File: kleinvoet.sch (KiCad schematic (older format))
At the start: 43 parts, among them CN1 Arduino_Conn, CN2 Arduino_Conn, CN3 Arduino_Conn, J1 Conn_ST_STDC14, SW1 RESET, SW2 RESET, U1 STM32F446RETx, U2 NOR Flash, Y1 12 MHz, Y2 32.768 kHz

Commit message: PCB Layout Checkpoint
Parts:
- added FB9: BLM15HD102SN1, Inductor_SMD:L_0402_1005Metric, symbol Device:Ferrite_Bead_Small
- SW2: value RESET -> USER
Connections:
- net +3V3: no longer CB6.1
- net A0: no longer CN1.1 (Pin_1)
- net A1: now also FB9.1; no longer CN1.2 (Pin_2)
- net A2: no longer CN1.3 (Pin_3)
- net A3: no longer CN1.4 (Pin_4)
- net A4: no longer CN1.5 (Pin_5)
- net A5: no longer CN1.6 (Pin_6)
- net D0: no longer CN3.8 (Pin_8)
- net D1: no longer CN3.7 (Pin_7)
- net D10: no longer CN2.8 (Pin_8)
- net D11: no longer CN2.7 (Pin_7)
- net D12: no longer CN2.6 (Pin_6)
- net D13: no longer CN2.5 (Pin_5)
- net D14: no longer CN2.2 (Pin_2)
- net D15: no longer CN2.1 (Pin_1)
- net D2: no longer CN3.6 (Pin_6)
- net D3: no longer CN3.5 (Pin_5)
- net D4: no longer CN3.4 (Pin_4)
- net D5: no longer CN3.3 (Pin_3)
- net D6: no longer CN3.2 (Pin_2)
- net D7: no longer CN3.1 (Pin_1)
- net D8: no longer CN2.10 (Pin_10)
- net D9: no longer CN2.9 (Pin_9)
- net USR_BTN: now also U1.28 (PB2)
- net VDD: now also CB6.1
- net ADC_~CS: now reaches U1.37 (PC6)
- new net GNSS_Module/GPS_RX: FB9.2
- no-connect marks 6 -> 26
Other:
- moved on the sheet: CB6
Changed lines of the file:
@@
-	1    0    0    -1
-$EndComp
-$Comp
-L Device:C_Small CB6
-U 1 1 5F161171
-P 5250 6000
-F 0 "CB6" H 5200 6300 50  0000 L CNN
-F 1 "100n" H 5150 6200 50  0000 L CNN
-F 2 "Capacitor_SMD:C_0603_1608Metric_Pad1.05x0.95mm_HandSolder" H 5250 6000 50  0001 C CNN
-F 3 "~" H 5250 6000 50  0001 C CNN
-F 4 "C0603C104M5RACTU" H 5250 6000 50  0001 C CNN "MPN"
-F 5 "KEMET" H 5250 6000 50  0001 C CNN "Mfr."
-	1    5250 6000
 	1    0    0    -1
 $EndComp
@@
 Wire Wire Line
 	4850 5900 5050 5900
-Connection ~ 5050 5900
-Wire Wire Line
-	5050 5900 5250 5900
 Wire Wire Line
 	4550 6100 4350 6100
 Connection ~ 4850 6100
-Connection ~ 5050 6100
 Wire Wire Line
 	5050 6100 4850 6100
-Wire Wire Line
-	5250 6100 5050 6100
 Wire Wire Line
 	4350 5900 4150 5900
@@
 	-1   0    0    -1
 $EndComp
-Text Label 3050 6800 0    50   ~ 0
-A0
-Text Label 3050 6900 0    50   ~ 0
-A1
-Text Label 3050 7000 0    50   ~ 0
-A2
-Text Label 3050 7100 0    50   ~ 0
-A3
-Text Label 3050 7200 0    50   ~ 0
-A4
-Text Label 3050 7300 0    50   ~ 0
-A5
 $Comp
 L Connector_Generic:Conn_01x10 CN2
@@
 	1    0    0    -1
 $EndComp
-Text Label 3750 6650 2    50   ~ 0
-D15
-Text Label 3750 6750 2    50   ~ 0
-D14
-Text Label 3750 7050 2    50   ~ 0
-D13
-Text Label 3750 7150 2    50   ~ 0
-D12
-Text Label 3750 7250 2    50   ~ 0
-D11
-Text Label 3750 7350 2    50   ~ 0
-D10
-Text Label 3750 7450 2    50   ~ 0
-D9
-Text Label 3750 7550 2    50   ~ 0
-D8
 $Comp
 L Connector_Generic:Conn_01x08 CN3
@@
 	1    0    0    -1
 $EndComp
-Text Label 4400 6750 2    50   ~ 0
-D7
-Text Label 4400 6850 2    50   ~ 0
-D6
-Text Label 4400 6950 2    50   ~ 0
-D5
-Text Label 4400 7050 2    50   ~ 0
-D4
-Text Label 4400 7150 2    50   ~ 0
-D3
-Text Label 4400 7250 2    50   ~ 0
-D2
-Text Label 4400 7350 2    50   ~ 0
-D1
-Text Label 4400 7450 2    50   ~ 0
-D0
 Wire Notes Line
 	2700 6500 4900 6500
@@
 Text Notes 5250 6500 0    50   ~ 10
 Status LEDs
-$Comp
-L MCU_ST_STM32F4:STM32F446RETx U1
-U 1 1 5EF8E42C
-P 4750 2950
-F 0 "U1" H 4250 1200 50  0000 C CNN
-F 1 "STM32F446RETx" H 5350 1200 50  0000 C CNN
-F 2 "Package_QFP:LQFP-64_10x10mm_P0.5mm" H 4150 1250 50  0001 R CNN
-F 3 "http://www.st.com/st-web-ui/static/active/en/resource/technical/document/datasheet/DM00141306.pdf" H 4750 2950 50  0001 C CNN
-F 4 "STM32F446RCT6" H 4750 2950 50  0001 C CNN "MPN"
-F 5 "STMicroelectronics" H 4750 2950 50  0001 C CNN "Mfr."
-	1    4750 2950
-	1    0    0    -1
-$EndComp
 $Comp
 L power:+3.3VA #PWR016
@@
 Wire Wire Line
 	2600 1500 2400 1500
-Wire Wire Line
-	2600 1700 2400 1700
 $Sheet
 S 1400 1350 1000 500
@@
 Wire Wire Line
 	2600 2200 2400 2200
-$Comp
-L power:GND #PWR03
-U 1 1 5EFC01A8
-P 2600 2550
-F 0 "#PWR03" H 2600 2300 50  0001 C CNN
-F 1 "GND" H 2605 2377 50  0000 C CNN
-F 2 "" H 2600 2550 50  0001 C CNN
-F 3 "" H 2600 2550 50  0001 C CNN
-	1    2600 2550
-	1    0    0    -1
-$EndComp
-Wire Wire Line
-	2600 2550 2600 2500
 Wire Wire Line
 	2600 2500 2400 2500
@@
 Wire Wire Line
 	1200 1750 1400 1750
+Text Label 5650 2350 0    50   ~ 0
+SDIO_WP
 Text Label 5650 2250 0    50   ~ 0
-SDIO_WP
-Text Label 5650 2350 0    50   ~ 0
 SDIO_CD
 Wire Wire Line
@@
 NoConn ~ 5450 2950
 NoConn ~ 5450 3850
-NoConn ~ 4050 3650
 Text Label 10650 5400 0    50   ~ 0
 OSC_LSE_IN
@@
 L power:VDD #PWR018
 U 1 1 5EEDB6FA
-P 5650 5900
-F 0 "#PWR018" H 5650 5750 50  0001 C CNN
-F 1 "VDD" H 5665 6073 50  0000 C CNN
-F 2 "" H 5650 5900 50  0001 C CNN
-F 3 "" H 5650 5900 50  0001 C CNN
-	1    5650 5900
+P 5550 5900
+F 0 "#PWR018" H 5550 5750 50  0001 C CNN
+F 1 "VDD" H 5565 6073 50  0000 C CNN
+F 2 "" H 5550 5900 50  0001 C CNN
+F 3 "" H 5550 5900 50  0001 C CNN
+	1    5550 5900
 	1    0    0    -1
 $EndComp
@@
 L power:GND #PWR019
 U 1 1 5EEDC419
-P 5650 6100
-F 0 "#PWR019" H 5650 5850 50  0001 C CNN
-F 1 "GND" H 5655 5927 50  0000 C CNN
-F 2 "" H 5650 6100 50  0001 C CNN
-F 3 "" H 5650 6100 50  0001 C CNN
-	1    5650 6100
+P 5550 6100
+F 0 "#PWR019" H 5550 5850 50  0001 C CNN
+F 1 "GND" H 5555 5927 50  0000 C CNN
+F 2 "" H 5550 6100 50  0001 C CNN
+F 3 "" H 5550 6100 50  0001 C CNN
+	1    5550 6100
 	1    0    0    -1
 $EndComp
@@
 Wire Wire Line
 	4050 4250 3850 4250
-NoConn ~ 5450 3350
 $Comp
 L Switch:SW_Push SW2
@@
 P 8800 1250
 F 0 "SW2" V 8800 1398 50  0000 L CNN
-F 1 "RESET" V 8845 1398 50  0001 L CNN
+F 1 "USER" V 8845 1398 50  0001 L CNN
 F 2 "grootvoet:SW_SPST_PTS647" H 8800 1450 50  0001 C CNN
 F 3 "~" H 8800 1450 50  0001 C CNN
@@
 Wire Wire Line
 	1200 2600 1400 2600
+$Comp
+L Device:Ferrite_Bead_Small FB9
+U 1 1 5F0F97AE
+P 2500 1700
+AR Path="/5F0F97AE" Ref="FB9"  Part="1"
+AR Path="/5EDF3693/5F0F97AE" Ref="FB?"  Part="1"
+F 0 "FB9" V 2650 1700 50  0000 C CNN
+F 1 "BLM15HD102SN1" V 2550 2050 50  0001 C CNN
+F 2 "Inductor_SMD:L_0402_1005Metric" V 2430 1700 50  0001 C CNN
+F 3 "~" H 2500 1700 50  0001 C CNN
+F 4 "BLM15HD102SN1D" V 2500 1700 50  0001 C CNN "MPN"
+F 5 "Murata Electronics" H 2500 1700 50  0001 C CNN "Mfr."
+	1    2500 1700
+	0    1    1    0
+$EndComp
+$Comp
+L Device:C_Small CB6
+U 1 1 5F161171
+P 5450 6000
+F 0 "CB6" H 5250 6100 50  0000 L CNN
+F 1 "100n" H 5200 6000 50  0000 L CNN
+F 2 "Capacitor_SMD:C_0603_1608Metric_Pad1.05x0.95mm_HandSolder" H 5450 6000 50  0001 C CNN
+F 3 "~" H 5450 6000 50  0001 C CNN
+F 4 "C0603C104M5RACTU" H 5450 6000 50  0001 C CNN "MPN"
+F 5 "KEMET" H 5450 6000 50  0001 C CNN "Mfr."
+	1    5450 6000
+	1    0    0    -1
+$EndComp
+Wire Wire Line
+	5450 5900 5550 5900
+Connection ~ 5550 5900
+Wire Wire Line
+	5550 5900 5650 5900
+Wire Wire Line
+	5650 6100 5550 6100
+Connection ~ 5550 6100
+Wire Wire Line
+	5550 6100 5450 6100
+Text Label 3850 3650 2    50   ~ 0
+ADC_~CS
+Wire Wire Line
+	4050 3650 3850 3650
+Text Label 2600 2500 0    50   ~ 0
+ADC_~CS
+Text Label 5650 3350 0    50   ~ 0
+USR_BTN
+$Comp
+L MCU_ST_STM32F4:STM32F446RETx U1
+U 1 1 5EF8E42C
+P 4750 2950
+F 0 "U1" H 4250 1200 50  0000 C CNN
+F 1 "STM32F446RETx" H 5350 1200 50  0000 C CNN
+F 2 "Package_QFP:LQFP-64_10x10mm_P0.5mm" H 4150 1250 50  0001 R CNN
+F 3 "http://www.st.com/st-web-ui/static/active/en/resource/technical/document/datasheet/DM00141306.pdf" H 4750 2950 50  0001 C CNN
+F 4 "STM32F446RCT6" H 4750 2950 50  0001 C CNN "MPN"
+F 5 "STMicroelectronics" H 4750 2950 50  0001 C CNN "Mfr."
+	1    4750 2950
+	1    0    0    -1
+$EndComp
+Wire Wire Line
+	5650 3350 5450 3350
+NoConn ~ 4400 6750
+NoConn ~ 4400 6850
+NoConn ~ 4400 6950
+NoConn ~ 4400 7050
+NoConn ~ 4400 7150
+NoConn ~ 4400 7250
+NoConn ~ 4400 7350
+NoConn ~ 4400 7450
+NoConn ~ 3750 7550
+NoConn ~ 3750 7450
+NoConn ~ 3750 7350
+NoConn ~ 3750 7250
+NoConn ~ 3750 7150
+NoConn ~ 3750 7050
+NoConn ~ 3750 6750
+NoConn ~ 3750 6650
+NoConn ~ 3050 6800
+NoConn ~ 3050 6900
+NoConn ~ 3050 7000
+NoConn ~ 3050 7100
+NoConn ~ 3050 7200
+NoConn ~ 3050 7300
 $EndSCHEMATC

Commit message: Major Commit with Final PCB Design
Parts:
- removed C3: 1u, Capacitor_SMD:C_0603_1608Metric_Pad1.05x0.95mm_HandSolder, symbol Device:C_Small
- removed CN1: Arduino_Conn, Connector_PinHeader_2.54mm:PinHeader_1x06_P2.54mm_Vertical, symbol Connector_Generic:Conn_01x06
- removed CN2: Arduino_Conn, Connector_PinHeader_2.54mm:PinHeader_1x10_P2.54mm_Vertical, symbol Connector_Generic:Conn_01x10
- removed CN3: Arduino_Conn, Connector_PinHeader_2.54mm:PinHeader_1x08_P2.54mm_Vertical, symbol Connector_Generic:Conn_01x08
- removed D2: GREEN, LED_SMD:LED_0603_1608Metric_Pad1.05x0.95mm_HandSolder, symbol Device:LED_Small
- removed D3: YELLOW, LED_SMD:LED_0603_1608Metric_Pad1.05x0.95mm_HandSolder, symbol Device:LED_Small
- removed R3, R4: 2.2k, Resistor_SMD:R_0603_1608Metric_Pad1.05x0.95mm_HandSolder, symbol Device:R_Small
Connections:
- net VDD is gone; now on net +3V3: CB6.1, U1.1 (VBAT)
- net D13: no longer R2.1
- net D15: now also CB9.1, SW2.1
- net RTC_CAL: no longer U1.2 (PC13)
- net LED_STATUS: now reaches U1.50 (PA15)
- net LED_STATUS: now also R2.1
- net D9 renamed ADC_CLK
- net GPS_WAKE: no longer names the net of U1.10 (PC2)
- net GPS_~SAFEBOOT: no longer names the net of U1.11 (PC3)
- removed net USR_BTN: CB9.1, SW2.1, U1.28 (PB2)
- no-connect marks 26 -> 7
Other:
- note removed: "Arduino Connectors"
- moved on the sheet: CB1, CB6, D1, R2, SW1

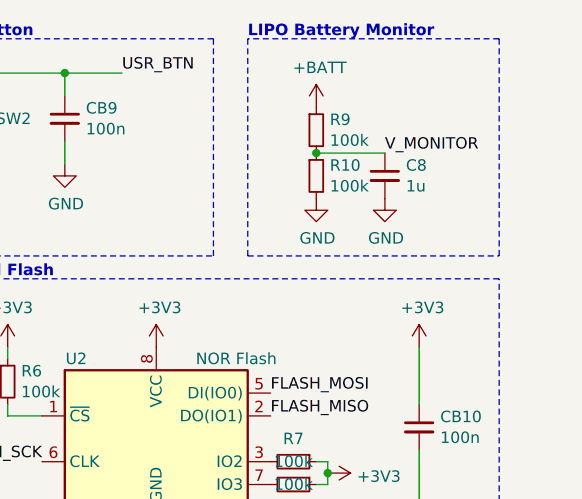
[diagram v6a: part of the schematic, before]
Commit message: Merge 'feature/mic-board'
Split out Sensor_board to own project for easier panelising later.
Allows also for better independent development.

Squashed commit of the following:
===============================================
commit 5c89ddf7514428c762fb7c211bc44fe947092eb1
Author: CM Geldenhuys <20198329@sun.ac.za>
Date:   Wed Oct 21 14:34:31 2020 +0200

    Add emblem

commit bbe0a53b49b0ec3aa4e2f65424c556ce99509fe4
Author: CM Geldenhuys <20198329@sun.ac.za>
Date:   Wed Oct 21 11:03:40 2020 +0200

    Misc.

commit b3172de48a622d4a7c8e9fb13a381d32a0990437
Author: CM Geldenhuys <20198329@sun.ac.za>
Date:   Wed Oct 21 08:26:42 2020 +0200

    Update BOM

commit e4c5b39694adfe3b823840b4cd3bc00d306b52fc
Author: CM Geldenhuys <20198329@sun.ac.za>
Date:   Wed Oct 21 07:26:34 2020 +0200

    Update Footprint & part num.

commit 6125562d7501cc555d98682860bdd64678a2fa40
Author: CM Geldenhuys <20198329@sun.ac.za>
Date:   Tue Oct 20 15:41:10 2020 +0200

    Misc. TODOs

commit 1431b8ace7af2c4960b7d9361ce6fcca694d3a38
Author: CM Geldenhuys <20198329@sun.ac.za>
Date:   Tue Oct 20 11:22:04 2020 +0200

    Update passives (fuse + Vsense)

commit 8105b403ec058cf7267c739b2e244ad8880c475f
Author: CM Geldenhuys <20198329@sun.ac.za>
Date:   Tue Oct 20 11:02:06 2020 +0200

    Flip GPS labels

commit f34b34dca70ce235e33188df7f6c69707ad79c9c
Author: CM Geldenhuys <20198329@sun.ac.za>
Date:   Tue Oct 20 10:58:45 2020 +0200

    Swap out ST-Link Conn

commit 1669b3f99c1cffa6c87811843550b346cfb9297e
Author: CM Geldenhuys <20198329@sun.ac.za>
Date:   Tue Oct 20 09:57:40 2020 +0200

    Update Sch with new compensation

commit dde033bb3cbd48a104931da2f1a7f681a8f96ac4
Author: CM Geldenhuys <20198329@sun.ac.za>
Date:   Tue Oct 20 09:55:04 2020 +0200

    Compensate for preamp loading on ADC driver

commit 2ddbd04fb1deccaa72131771362207bd14115936
Author: CM Geldenhuys <20198329@sun.ac.za>
Date:   Tue Oct 20 09:38:09 2020 +0200

    Compensate for buffer output impedance

commit 2f74ea7d6b171bacb6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
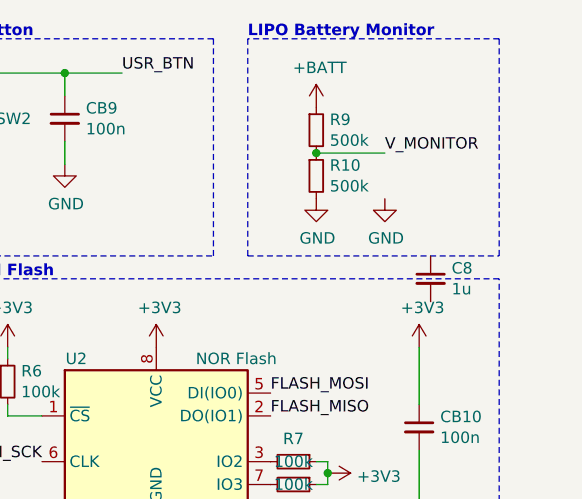
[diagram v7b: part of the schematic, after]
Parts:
- C4, C5, C6, C7, C8, C9, CB1, CB10, CB2, CB3, CB4, CB5, CB6, CB7, CB8, CB9: footprint Capacitor_SMD:C_0603_1608Metric_Pad1.05x0.95mm_HandSolder -> Capacitor_SMD:C_0603_1608Metric_Pad1.08x0.95mm_HandSolder
- J1: footprint Connector_PinHeader_1.27mm:PinHeader_2x07_P1.27mm_Vertical -> grootvoet:SAMTEC-FTSH-107-01-X-D
- R10, R9: value 100k -> 500k; MPN RC0603FR-07100KL -> (none); Mfr. Yageo -> (none)
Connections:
- net ADC1_IN9: no longer C8.1
- net GND: no longer C8.2
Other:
- moved on the sheet: C8
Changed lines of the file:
@@
 $Descr A4 11693 8268
 encoding utf-8
-Sheet 1 17
+Sheet 1 13
 Title "Kleinvoet"
 Date "2020-06-11"
@@
 F 0 "CB2" H 4300 6300 50  0000 L CNN
 F 1 "100n" H 4250 6200 50  0000 L CNN
-F 2 "Capacitor_SMD:C_0603_1608Metric_Pad1.05x0.95mm_HandSolder" H 4350 6000 50  0001 C CNN
+F 2 "Capacitor_SMD:C_0603_1608Metric_Pad1.08x0.95mm_HandSolder" H 4350 6000 50  0001 C CNN
 F 3 "~" H 4350 6000 50  0001 C CNN
 F 4 "C0603C104M5RACTU" H 4350 6000 50  0001 C CNN "MPN"
@@
 F 0 "CB7" H 7942 5841 50  0000 L CNN
 F 1 "100n" H 7942 5750 50  0000 L CNN
-F 2 "Capacitor_SMD:C_0603_1608Metric_Pad1.05x0.95mm_HandSolder" H 7850 5750 50  0001 C CNN
+F 2 "Capacitor_SMD:C_0603_1608Metric_Pad1.08x0.95mm_HandSolder" H 7850 5750 50  0001 C CNN
 F 3 "~" H 7850 5750 50  0001 C CNN
 F 4 "Low ESR (X7R)" H 7942 5659 50  0000 L CNN "Notes"
@@
 F 0 "C4" H 7192 5841 50  0000 L CNN
 F 1 "1u" H 7192 5750 50  0000 L CNN
-F 2 "Capacitor_SMD:C_0603_1608Metric_Pad1.05x0.95mm_HandSolder" H 7100 5750 50  0001 C CNN
+F 2 "Capacitor_SMD:C_0603_1608Metric_Pad1.08x0.95mm_HandSolder" H 7100 5750 50  0001 C CNN
 F 3 "~" H 7100 5750 50  0001 C CNN
 F 4 "Low ESR (X7R)" H 7192 5659 50  0000 L CNN "Notes"
@@
 F 0 "CB8" H 8692 5841 50  0000 L CNN
 F 1 "10n" H 8692 5750 50  0000 L CNN
-F 2 "Capacitor_SMD:C_0603_1608Metric_Pad1.05x0.95mm_HandSolder" H 8600 5750 50  0001 C CNN
+F 2 "Capacitor_SMD:C_0603_1608Metric_Pad1.08x0.95mm_HandSolder" H 8600 5750 50  0001 C CNN
 F 3 "~" H 8600 5750 50  0001 C CNN
 F 4 "Low ESR (X7R)" H 8692 5659 50  0000 L CNN "Notes"
@@
 F 0 "CB3" H 4500 6300 50  0000 L CNN
 F 1 "100n" H 4450 6200 50  0000 L CNN
-F 2 "Capacitor_SMD:C_0603_1608Metric_Pad1.05x0.95mm_HandSolder" H 4550 6000 50  0001 C CNN
+F 2 "Capacitor_SMD:C_0603_1608Metric_Pad1.08x0.95mm_HandSolder" H 4550 6000 50  0001 C CNN
 F 3 "~" H 4550 6000 50  0001 C CNN
 F 4 "C0603C104M5RACTU" H 4550 6000 50  0001 C CNN "MPN"
@@
 F 0 "CB4" H 4800 6300 50  0000 L CNN
 F 1 "100n" H 4750 6200 50  0000 L CNN
-F 2 "Capacitor_SMD:C_0603_1608Metric_Pad1.05x0.95mm_HandSolder" H 4850 6000 50  0001 C CNN
+F 2 "Capacitor_SMD:C_0603_1608Metric_Pad1.08x0.95mm_HandSolder" H 4850 6000 50  0001 C CNN
 F 3 "~" H 4850 6000 50  0001 C CNN
 F 4 "C0603C104M5RACTU" H 4850 6000 50  0001 C CNN "MPN"
@@
 F 0 "CB5" H 5000 6300 50  0000 L CNN
 F 1 "100n" H 4950 6200 50  0000 L CNN
-F 2 "Capacitor_SMD:C_0603_1608Metric_Pad1.05x0.95mm_HandSolder" H 5050 6000 50  0001 C CNN
+F 2 "Capacitor_SMD:C_0603_1608Metric_Pad1.08x0.95mm_HandSolder" H 5050 6000 50  0001 C CNN
 F 3 "~" H 5050 6000 50  0001 C CNN
 F 4 "C0603C104M5RACTU" H 5050 6000 50  0001 C CNN "MPN"
@@
 F 0 "CB1" H 4492 7196 50  0000 L CNN
 F 1 "100n" H 4492 7105 50  0000 L CNN
-F 2 "Capacitor_SMD:C_0603_1608Metric_Pad1.05x0.95mm_HandSolder" H 4400 7150 50  0001 C CNN
+F 2 "Capacitor_SMD:C_0603_1608Metric_Pad1.08x0.95mm_HandSolder" H 4400 7150 50  0001 C CNN
 F 3 "~" H 4400 7150 50  0001 C CNN
 F 4 "C0603C104M5RACTU" H 4400 7150 50  0001 C CNN "MPN"
@@
 F 0 "J1" H 1207 6696 50  0000 R CNN
 F 1 "Conn_ST_STDC14" H 1207 6605 50  0000 R CNN
-F 2 "Connector_PinHeader_1.27mm:PinHeader_2x07_P1.27mm_Vertical" H 1650 6650 50  0001 C CNN
+F 2 "grootvoet:SAMTEC-FTSH-107-01-X-D" H 1650 6650 50  0001 C CNN
 F 3 "https://www.st.com/content/ccc/resource/technical/document/user_manual/group1/99/49/91/b6/b2/3a/46/e5/DM00526767/files/DM00526767.pdf/jcr:content/translations/en.DM00526767.pdf" V 1300 5400 50  0001 C CNN
 F 4 "M50-055023W0445" H 1650 6650 50  0001 C CNN "MPN"
@@
 F 0 "C5" H 8092 4296 50  0000 L CNN
 F 1 "15pF" H 8092 4205 50  0000 L CNN
-F 2 "Capacitor_SMD:C_0603_1608Metric_Pad1.05x0.95mm_HandSolder" H 8000 4250 50  0001 C CNN
+F 2 "Capacitor_SMD:C_0603_1608Metric_Pad1.08x0.95mm_HandSolder" H 8000 4250 50  0001 C CNN
 F 3 "~" H 8000 4250 50  0001 C CNN
 F 4 "C0G - High freq." H 8000 4250 50  0001 C CNN "Notes"
@@
 F 0 "C6" H 8642 4296 50  0000 L CNN
 F 1 "15pF" H 8642 4205 50  0000 L CNN
-F 2 "Capacitor_SMD:C_0603_1608Metric_Pad1.05x0.95mm_HandSolder" H 8550 4250 50  0001 C CNN
+F 2 "Capacitor_SMD:C_0603_1608Metric_Pad1.08x0.95mm_HandSolder" H 8550 4250 50  0001 C CNN
 F 3 "~" H 8550 4250 50  0001 C CNN
 F 4 "C0G - High freq." H 8550 4250 50  0001 C CNN "Notes"
@@
 F 0 "C7" H 10192 5696 50  0000 L CNN
 F 1 "4p" H 10192 5605 50  0000 L CNN
-F 2 "Capacitor_SMD:C_0603_1608Metric_Pad1.05x0.95mm_HandSolder" H 10100 5650 50  0001 C CNN
+F 2 "Capacitor_SMD:C_0603_1608Metric_Pad1.08x0.95mm_HandSolder" H 10100 5650 50  0001 C CNN
 F 3 "~" H 10100 5650 50  0001 C CNN
 F 4 "C0G" H 10100 5650 50  0001 C CNN "Notes"
@@
 F 0 "C9" H 10742 5696 50  0000 L CNN
 F 1 "4p" H 10742 5605 50  0000 L CNN
-F 2 "Capacitor_SMD:C_0603_1608Metric_Pad1.05x0.95mm_HandSolder" H 10650 5650 50  0001 C CNN
+F 2 "Capacitor_SMD:C_0603_1608Metric_Pad1.08x0.95mm_HandSolder" H 10650 5650 50  0001 C CNN
 F 3 "~" H 10650 5650 50  0001 C CNN
 F 4 "C0G" H 10650 5650 50  0001 C CNN "Notes"
@@
 F 0 "CB10" H 10892 2646 50  0000 L CNN
 F 1 "100n" H 10892 2555 50  0000 L CNN
-F 2 "Capacitor_SMD:C_0603_1608Metric_Pad1.05x0.95mm_HandSolder" H 10800 2600 50  0001 C CNN
+F 2 "Capacitor_SMD:C_0603_1608Metric_Pad1.08x0.95mm_HandSolder" H 10800 2600 50  0001 C CNN
 F 3 "~" H 10800 2600 50  0001 C CNN
 F 4 "C0603C104M5RACTU" H 10800 2600 50  0001 C CNN "MPN"
@@
 P 10350 1300
 F 0 "R9" H 10409 1346 50  0000 L CNN
-F 1 "100k" H 10409 1255 50  0000 L CNN
+F 1 "500k" H 10409 1255 50  0000 L CNN
 F 2 "Resistor_SMD:R_0603_1608Metric_Pad1.05x0.95mm_HandSolder" H 10350 1300 50  0001 C CNN
 F 3 "~" H 10350 1300 50  0001 C CNN
-F 4 "RC0603FR-07100KL" H 10350 1300 50  0001 C CNN "MPN"
-F 5 "Yageo" H 10350 1300 50  0001 C CNN "Mfr."
+F 4 "" H 10350 1300 50  0001 C CNN "MPN"
+F 5 "" H 10350 1300 50  0001 C CNN "Mfr."
 	1    10350 1300
 	1    0    0    -1
@@
 P 10350 1500
 F 0 "R10" H 10409 1546 50  0000 L CNN
-F 1 "100k" H 10409 1455 50  0000 L CNN
+F 1 "500k" H 10409 1455 50  0000 L CNN
 F 2 "Resistor_SMD:R_0603_1608Metric_Pad1.05x0.95mm_HandSolder" H 10350 1500 50  0001 C CNN
 F 3 "~" H 10350 1500 50  0001 C CNN
-F 4 "RC0603FR-07100KL" H 10350 1500 50  0001 C CNN "MPN"
-F 5 "Yageo" H 10350 1500 50  0001 C CNN "Mfr."
+F 4 "" H 10350 1500 50  0001 C CNN "MPN"
+F 5 "" H 10350 1500 50  0001 C CNN "Mfr."
 	1    10350 1500
 	1    0    0    -1
@@
 L Device:C_Small C8
 U 1 1 5EF88144
-P 10650 1500
-F 0 "C8" H 10742 1546 50  0000 L CNN
-F 1 "1u" H 10742 1455 50  0000 L CNN
-F 2 "Capacitor_SMD:C_0603_1608Metric_Pad1.05x0.95mm_HandSolder" H 10650 1500 50  0001 C CNN
-F 3 "~" H 10650 1500 50  0001 C CNN
-F 4 "C0603C105K8RACTU" H 10650 1500 50  0001 C CNN "MPN"
-F 5 "KEMET" H 10650 1500 50  0001 C CNN "Mfr."
-	1    10650 1500
+P 10850 1950
+F 0 "C8" H 10942 1996 50  0000 L CNN
+F 1 "1u" H 10942 1905 50  0000 L CNN
+F 2 "Capacitor_SMD:C_0603_1608Metric_Pad1.08x0.95mm_HandSolder" H 10850 1950 50  0001 C CNN
+F 3 "~" H 10850 1950 50  0001 C CNN
+F 4 "C0603C105K8RACTU" H 10850 1950 50  0001 C CNN "MPN"
+F 5 "KEMET" H 10850 1950 50  0001 C CNN "Mfr."
+	1    10850 1950
 	1    0    0    -1
 $EndComp
@@
 F 0 "CB9" H 9342 1296 50  0000 L CNN
 F 1 "100n" H 9342 1205 50  0000 L CNN
-F 2 "Capacitor_SMD:C_0603_1608Metric_Pad1.05x0.95mm_HandSolder" H 9250 1250 50  0001 C CNN
+F 2 "Capacitor_SMD:C_0603_1608Metric_Pad1.08x0.95mm_HandSolder" H 9250 1250 50  0001 C CNN
 F 3 "~" H 9250 1250 50  0001 C CNN
 F 4 "C0603C104M5RACTU" H 9250 1250 50  0001 C CNN "MPN"
@@
 F 0 "CB6" H 5200 6300 50  0000 L CNN
 F 1 "100n" H 5150 6200 50  0000 L CNN
-F 2 "Capacitor_SMD:C_0603_1608Metric_Pad1.05x0.95mm_HandSolder" H 5250 6000 50  0001 C CNN
+F 2 "Capacitor_SMD:C_0603_1608Metric_Pad1.08x0.95mm_HandSolder" H 5250 6000 50  0001 C CNN
 F 3 "~" H 5250 6000 50  0001 C CNN
 F 4 "C0603C104M5RACTU" H 5250 6000 50  0001 C CNN "MPN"
